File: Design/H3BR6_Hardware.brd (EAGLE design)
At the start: 60 x 34.6 mm, 64 parts, among them P2 HEXABIT_X2_P1_P5, Q10 MMBT3904LT1, Q11 MMBT3904LT1, Q12 MMBT3904LT1, Q13 MMBT3904LT1, Q14 MMBT3904LT1, Q7 MMBT3904LT1, Q8 MMBT3904LT1, Q9 MMBT3904LT1, U1 STM32F072CBT6STMICROELECTRONI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, X1 XTALL_CSTCE8M00G52

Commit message: Finishing PCB
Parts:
- moved C3 1.28 mm to (8.73, 14.0)
- moved C4 0.57 mm to (10.2, 11.9)
- moved R12 0.50 mm to (23.3, 27.1)
- moved B 0.45 mm to (4.76, 18.7), turned to 270 degrees
- moved R10 0.35 mm to (11.0, 16.2)
- moved Q13 0.35 mm to (14.4, 15.2)
- moved R3 0.35 mm to (3.65, 21.3)
- moved C6 0.32 mm to (18.7, 16.5)
- moved C7 0.32 mm to (18.7, 16.2)
- moved R 0.32 mm to (14.6, 34.0)
- moved C 0.16 mm to (5.87, 15.6)
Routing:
- net GND: track 125.7 -> 117.3 mm, vias 8 -> 7
- net DP: track 37.2 -> 34.0 mm
- net USART2_TX: track 23.7 -> 20.7 mm
- net C_LED: track 48.5 -> 45.5 mm
- net C: track 41.1 -> 38.2 mm
- net CA4: track 41.8 -> 39.0 mm
- net D: track 31.1 -> 28.8 mm
- net VDD: track 79.7 -> 81.9 mm
- net USART1_RX: track 19.8 -> 17.7 mm
- net A: track 8.80 -> 6.84 mm
- net N$42: track 23.7 -> 21.7 mm
- net CA1: track 38.6 -> 36.8 mm
- net USART1_TX: track 17.6 -> 15.9 mm
- net N$37: track 28.5 -> 26.9 mm
- net USART3_RX: track 18.6 -> 17.1 mm
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
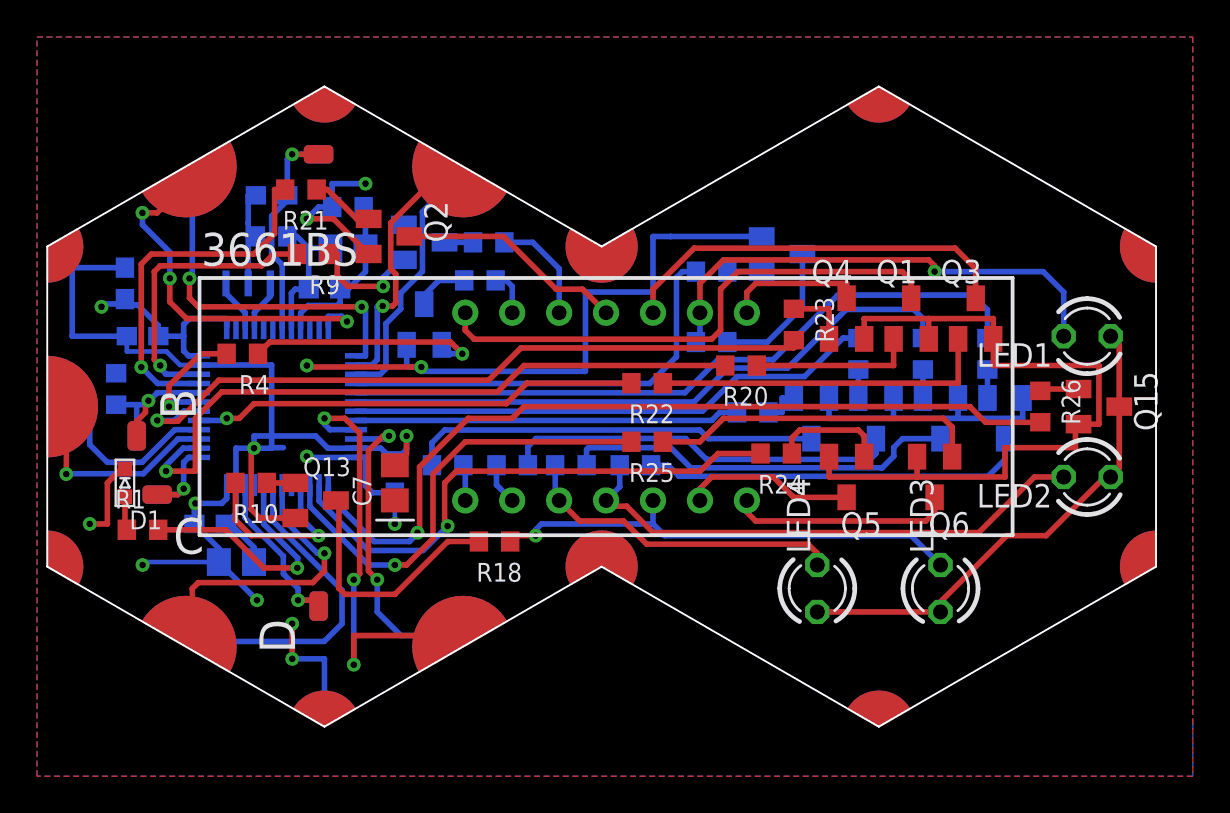
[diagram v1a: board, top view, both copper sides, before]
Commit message: Fix Wire Width
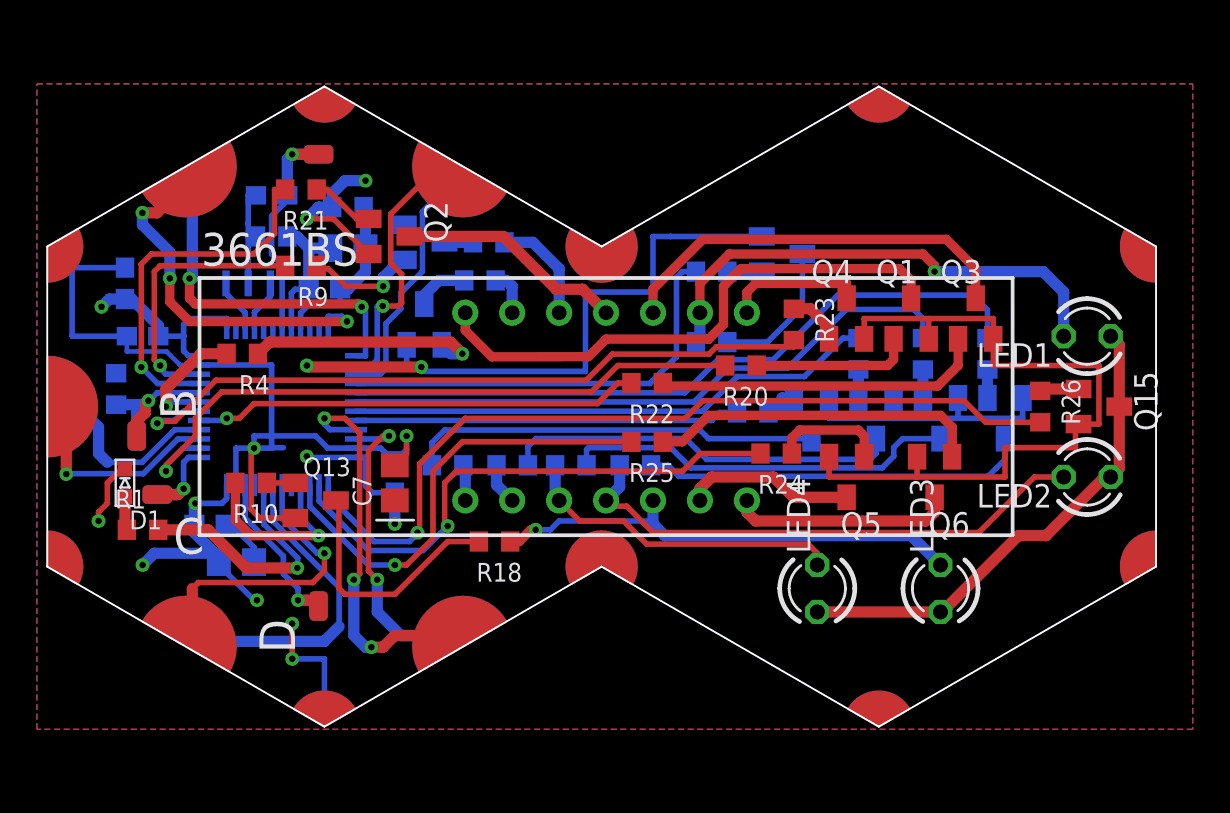
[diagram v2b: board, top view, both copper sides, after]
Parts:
- moved R9 0.90 mm to (13.7, 27.9)
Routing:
- net USART3_TX: track 24.2 -> 21.6 mm
- net CA1: track 36.8 -> 35.9 mm
- net GND: track 117.3 -> 116.4 mm
- net F: track 15.7 -> 14.8 mm
- net N$44: track 29.3 -> 30.1 mm
- net USART6_TX: track 14.2 -> 15.0 mm
- net N$28: track 3.54 -> 2.95 mm

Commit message: Final Design REV 1
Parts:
- moved LED4 1.42 mm to (41.0, 9.21)
- moved LED3 1.31 mm to (48.6, 9.21)
- moved C 0.16 mm to (5.87, 15.4)
- flipped R to the top
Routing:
- net N$46: track 26.9 -> 28.8 mm
- net N$32: track 25.9 -> 26.8 mm
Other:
- board text added: "*P1"
- board text added: "P2"
- board text added: "P3"
- board text added: "P4"
- board text added: "P5"
